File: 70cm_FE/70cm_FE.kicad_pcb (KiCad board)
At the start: 2 copper layers, 50 x 70 mm, 150 parts, among them J2 U.FL, J3 U.FL, J4 U.FL, Q1 2SC3356, Q2 2SC3356, Q3 2SC3356, U1 HT7533-1, U2 74HC14, U3 74HC14, U4 LM393, U5 M68710L

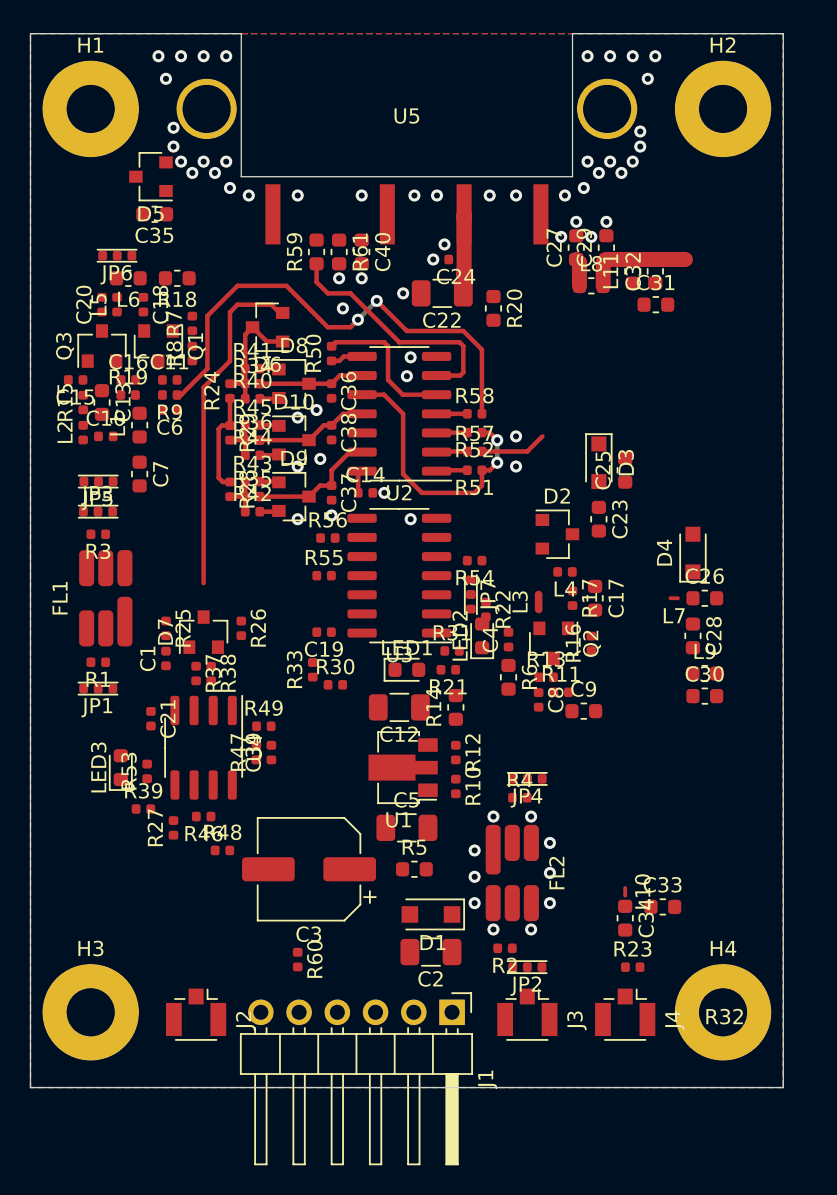
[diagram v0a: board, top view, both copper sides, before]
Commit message: Add RF filtering details and other small additions
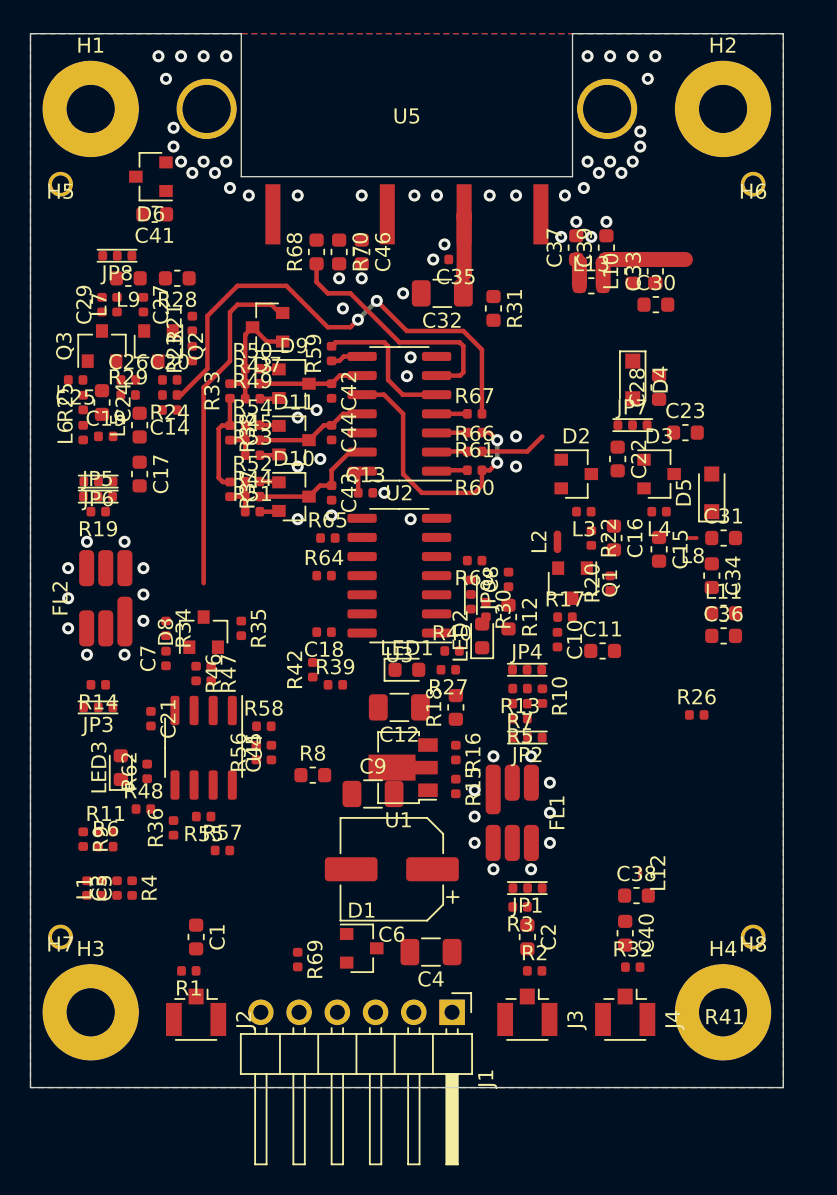
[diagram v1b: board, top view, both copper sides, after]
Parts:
- removed the C4 at (131.8, 90.2)
- added C1: 100p, Capacitor_SMD:C_0603_1608Metric, F.Cu at (111.0, 110.0)
- added C15: 10p, Capacitor_SMD:C_0603_1608Metric, F.Cu at (141.8, 84.2)
- added C2: 100p, Capacitor_SMD:C_0603_1608Metric, F.Cu at (133.0, 110.0)
- added C23: 10p, Capacitor_SMD:C_0603_1608Metric, F.Cu at (143.5, 76.5)
- added C3: 4p7, Capacitor_SMD:C_0402_1005Metric, F.Cu at (105.8, 106.8)
- added C5: DNP, Capacitor_SMD:C_0402_1005Metric, F.Cu at (103.8, 106.8)
- added C8: 1n, Capacitor_SMD:C_0402_1005Metric, F.Cu at (131.8, 86.2)
- added D3: BAV99, Package_TO_SOT_SMD:SOT-23, F.Cu at (141.8, 79.2)
- added H5: Tooling hole, 70cm_FE:JLCPCB_ToolingHole, F.Cu at (102.0, 60.0)
- added H6: Tooling hole, 70cm_FE:JLCPCB_ToolingHole, F.Cu at (148.0, 60.0)
- added H7: Tooling hole, 70cm_FE:JLCPCB_ToolingHole, F.Cu at (102.0, 110.0)
- added H8: Tooling hole, 70cm_FE:JLCPCB_ToolingHole, F.Cu at (148.0, 110.0)
- added JP4: ~, 70cm_FE:Jumper-3_0402, F.Cu at (132.5, 92.2)
- added JP7: ~, 70cm_FE:Jumper-3_0402, F.Cu at (139.5, 76.0)
- added L1: 15n, Inductor_SMD:L_0402_1005Metric, F.Cu at (104.8, 106.8)
- added L4: 15n, Inductor_SMD:L_0402_1005Metric, F.Cu at (141.8, 81.8)
- added R1: 100k, Resistor_SMD:R_0402_1005Metric, F.Cu at (110.5, 112.2)
- added R11: DNP, Resistor_SMD:R_0402_1005Metric, F.Cu at (105.0, 103.0)
- added R13: DNP, Resistor_SMD:R_0402_1005Metric, F.Cu at (132.5, 93.5)
- added R2: 100k, Resistor_SMD:R_0402_1005Metric, F.Cu at (133.5, 112.2)
- added R26: 100k, Resistor_SMD:R_0402_1005Metric, F.Cu at (144.2, 95.2)
- added R4: 47, Resistor_SMD:R_0402_1005Metric, F.Cu at (106.8, 106.8)
- added R6: DNP, Resistor_SMD:R_0402_1005Metric, F.Cu at (105.0, 104.0)
- added R7: DNP, Resistor_SMD:R_0402_1005Metric, F.Cu at (132.5, 94.5)
- added R9: 0, Resistor_SMD:R_0402_1005Metric, F.Cu at (103.5, 103.5)
- C7: renamed from C1; value 1p -> 4p7
- D1: value SM4007PL -> BAV99; footprint Diode_SMD:D_SOD-123F -> Package_TO_SOT_SMD:SOT-23
- D8: renamed from D7; value BAT54C -> BAS70-05
- L12: renamed from L10; value 23 mm -> 22 mm
- L8: renamed from L7; value 24 mm -> 26 mm
- moved R8 9.20 mm to (118.8, 99.2)
- moved C28 5.94 mm to (141.8, 73.5)
- moved D4 5.94 mm to (140.0, 73.0)
- moved C6 5.50 mm to (124.0, 105.5)
- moved JP1 5.25 mm to (133.5, 106.8)
- moved R5 5.25 mm to (132.5, 95.5), turned to 180 degrees
- moved D1 5.12 mm to (122.0, 110.8), turned to 0 degrees
- moved C10 4.19 mm to (135.0, 90.2)
- moved C11 4.19 mm to (138.0, 91.0)
- moved C16 4.19 mm to (138.8, 83.5)
- moved C22 4.19 mm to (139.0, 78.2)
- moved C31 4.19 mm to (146.0, 83.5)
- moved C34 4.19 mm to (145.2, 86.0)
- moved C36 4.19 mm to (146.0, 90.0)
- moved D2 4.19 mm to (136.2, 79.2)
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- renumbered C8 to C10, C9 to C11, C14 to C13, C6 to C14, C17 to C16, C7 to C17, C19 to C18, C10 to C19, C11 to C20, C23 to C22, C13 to C24, C15 to C25, C16 to C26, C18 to C27, C25 to C28, C20 to C29, C31 to C30, C26 to C31, C22 to C32, C32 to C33, C28 to C34, C24 to C35, C30 to C36, C27 to C37, C33 to C38, C29 to C39, C2 to C4, C34 to C40, C35 to C41, C36 to C42, C37 to C43, C38 to C44, C39 to C45, C40 to C46, C3 to C6, C5 to C9, D9 to D10, D10 to D11, D3 to D4, D4 to D5, D5 to D6, D6 to D7, D8 to D9, FL2 to FL1, FL1 to FL2, JP2 to JP1, JP4 to JP2, JP1 to JP3, JP3 to JP5, JP5 to JP6, JP6 to JP8, JP7 to JP9, L11 to L10, L9 to L11, L8 to L13, L3 to L2, L4 to L3, L1 to L5, L2 to L6, L5 to L7, L6 to L9, Q2 to Q1, Q1 to Q2, R11 to R10, R6 to R12, R1 to R14, R10 to R15, R12 to R16, R13 to R17, R14 to R18, R3 to R19, R16 to R20, R7 to R21, R17 to R22, R8 to R23, R9 to R24, R15 to R25, R21 to R27, R18 to R28, R19 to R29, R2 to R3, R22 to R30, R20 to R31, R23 to R32, R24 to R33, R25 to R34, R26 to R35, R27 to R36, R28 to R37, R29 to R38, R30 to R39, R31 to R40, R32 to R41, R33 to R42, R34 to R43, R35 to R44, R36 to R45, R37 to R46, R38 to R47, R39 to R48, R40 to R49, R4 to R5, R41 to R50, R42 to R51, R43 to R52, R44 to R53, R45 to R54, R46 to R55, R47 to R56, R48 to R57, R49 to R58, R50 to R59, R51 to R60, R52 to R61, R53 to R62, R54 to R63, R55 to R64, R56 to R65, R57 to R66, R58 to R67, R59 to R68, R60 to R69, R61 to R70, R5 to R8
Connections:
- C11 pad 1: Net-(C9-Pad1) (its old number) -> /LNA_C
- C22 pad 1: /PIN_RXRF -> /LNA_IN
- C7 pad 1: /TX -> Net-(C5-Pad1)
- D1 pad 1: /V_in -> GND
- D1 pad 2: GND -> /V_in
- JP1 pad 2: /RX -> Net-(C2-Pad1)
- JP2 pad 2: /LNA_OUT -> Net-(JP2-Pad2)
- JP3 pad 1: /TXSAW_in -> /TXSAW_bypass
- JP3 pad 2: /TX -> Net-(JP3-Pad2)
- JP3 pad 3: /TXSAW_bypass -> /TXSAW_in
- JP5 pad 2: Net-(JP3-Pad2) -> /TX_filtered
- JP6 pad 2: Net-(JP3-Pad2) -> /TX_filtered
- R10 pad 1: /LNA_C -> Net-(JP4-Pad2)
- R10 pad 2: Net-(C9-Pad1) (its old number) -> Net-(JP2-Pad2)
- R14 pad 1: /TXSAW_in -> Net-(JP3-Pad2)
- R19 pad 1: /TXSAW_out -> /TX_filtered
- R3 pad 1: /RXSAW_OUT -> Net-(C2-Pad1)
- R5 pad 1: /RXSAW_IN -> Net-(JP2-Pad2)
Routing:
- net GND: vias 66 -> 76

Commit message: Do some layout for 70 cm frontend
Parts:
- moved R41 40.2 mm to (114.0, 92.2), turned to 90 degrees
- moved D8 15.6 mm to (110.2, 105.2), turned to 270 degrees
- moved R40 15.1 mm to (113.0, 92.2), turned to 270 degrees
- moved R35 13.2 mm to (111.8, 102.5)
- moved R34 13.0 mm to (108.8, 102.5)
- moved R57 12.0 mm to (112.0, 92.2), turned to 270 degrees
- moved C7 11.6 mm to (107.2, 103.0), turned to 0 degrees
- moved C45 11.1 mm to (117.2, 86.8)
- moved R56 11.1 mm to (116.2, 86.8)
- moved R36 11.0 mm to (110.5, 91.8), turned to 180 degrees
- moved R46 10.1 mm to (109.8, 102.5), turned to 90 degrees
- moved R47 10.1 mm to (110.8, 102.5), turned to 90 degrees
- moved R48 9.37 mm to (109.0, 92.2), turned to 270 degrees
- moved R55 9.30 mm to (110.5, 92.8)
- moved C21 8.75 mm to (113.2, 102.5)
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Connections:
- D8 pad 1: /DET_RF -> /DET_REF
- D8 pad 2: /DET_REF -> /DET_RF
- U4 pad 1: /DET_COMPout -> /~OverTemp~
- U4 pad 2: /DET_COMP- -> /TempLimit
- U4 pad 3: /DET_COMP+ -> /TempHysteresis
- U4 pad 5: /TempHysteresis -> /DET_COMP+
- U4 pad 6: /TempLimit -> /DET_COMP-
- U4 pad 7: /~OverTemp~ -> /DET_COMPout
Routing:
- net /~OverTemp~: track 22.7 -> 30.4 mm
- net /VDD: track 1.55 -> 7.24 mm
- net /PA_VDD: track 4.32 -> 0.37 mm
- net /TempHysteresis: track 0.00 -> 3.58 mm
- net /TempLimit: track 0.00 -> 3.58 mm
- net /DET_RF: track 0.00 -> 3.47 mm
- net /DET_REF: track 0.00 -> 2.45 mm
- net /DET_COMP+: track 0.00 -> 2.17 mm
- net /DET_COMP-: track 0.00 -> 2.16 mm
- net /TempSensor: track 0.00 -> 1.02 mm
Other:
- outline, holes or cut-outs redrawn

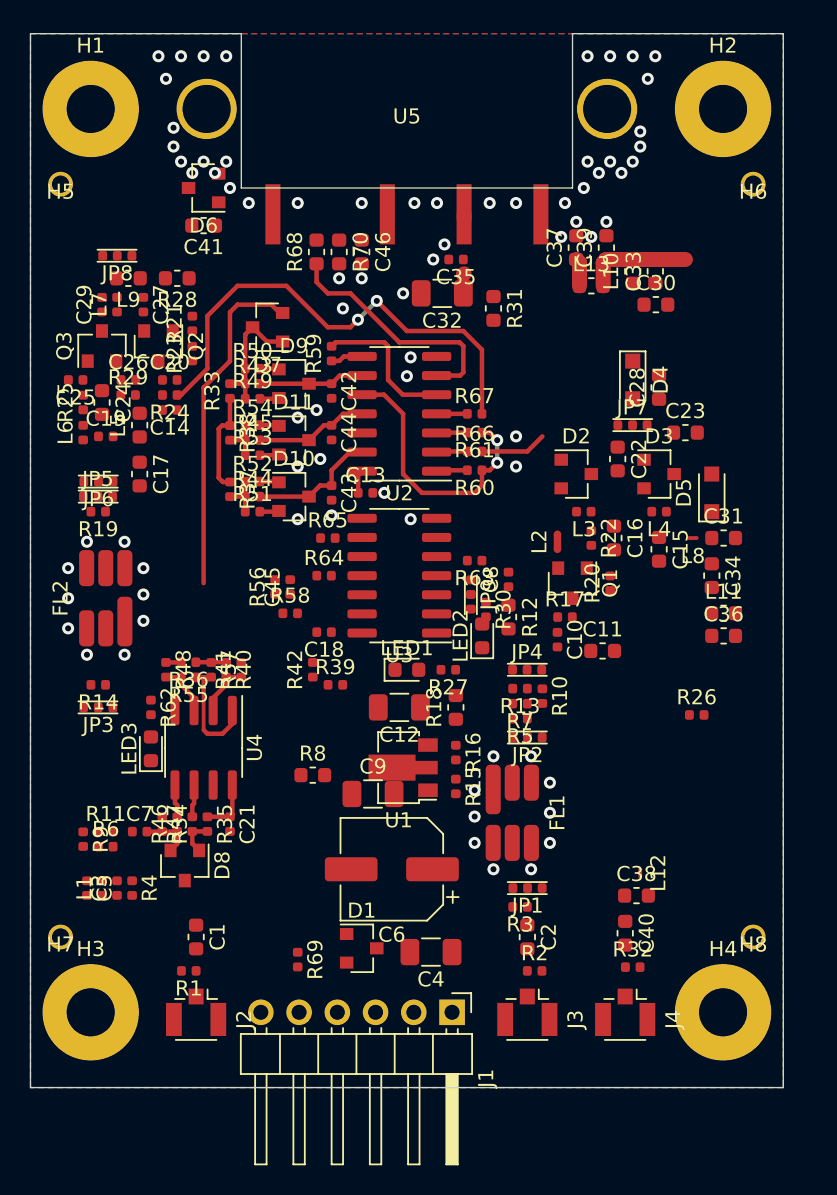
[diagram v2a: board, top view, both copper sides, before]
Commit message: More 70 cm frontend layout
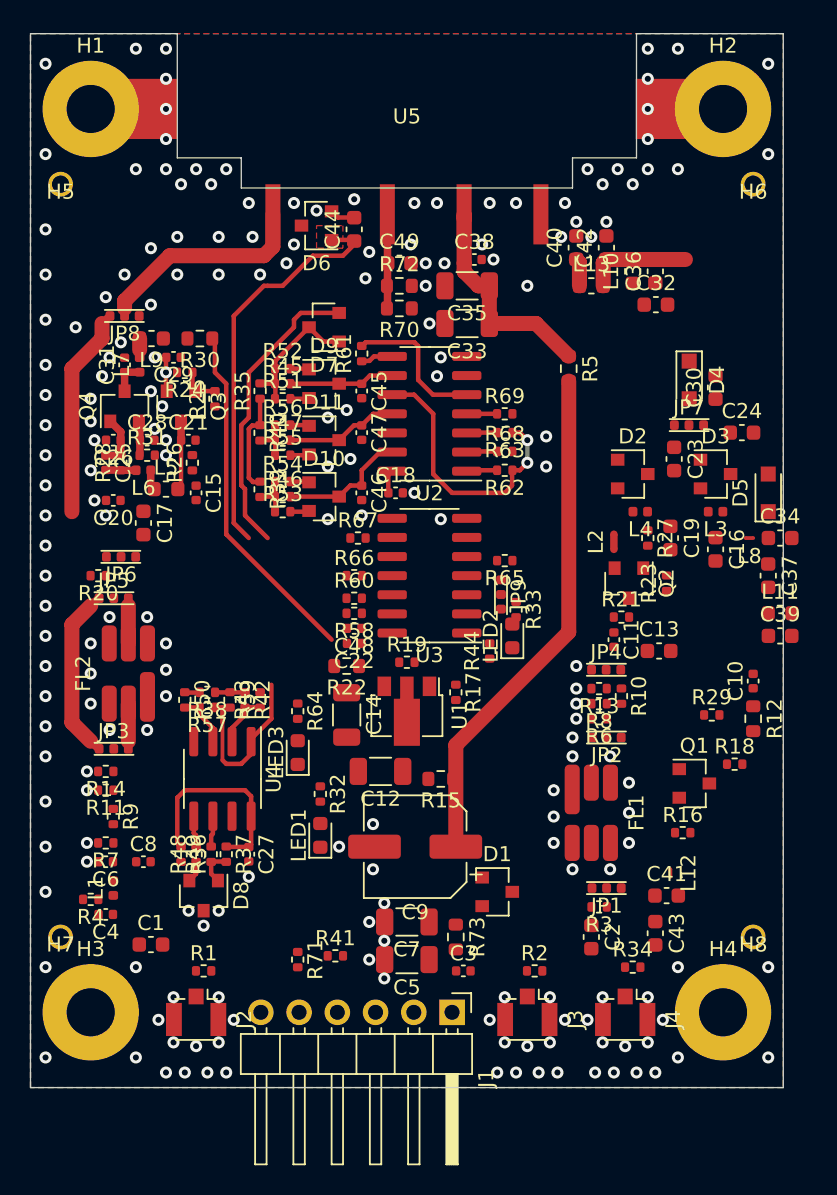
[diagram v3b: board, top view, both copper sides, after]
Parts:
- removed the C14 at (109.2, 75.0)
- removed the C19 at (105.0, 76.8)
- removed the C24 at (104.8, 74.5)
- removed the C8 at (131.8, 86.2)
- removed the Q2 at (108.5, 70.8)
- removed the R19 at (104.5, 81.8)
- removed the R21 at (110.8, 69.2)
- removed the R23 at (110.8, 71.2)
- removed the R29 at (106.5, 74.0)
- removed the R34 at (108.8, 102.5)
- removed the R35 at (111.8, 102.5)
- removed the R40 at (113.0, 92.2)
- removed the R41 at (114.0, 92.2)
- removed the R46 at (109.8, 102.5)
- removed the R47 at (110.8, 102.5)
- removed the R55 at (110.5, 92.8)
- removed the R62 at (108.0, 94.8)
- added C10: 1n, Capacitor_SMD:C_0402_1005Metric, F.Cu at (148.0, 93.0)
- added C15: 1n, Capacitor_SMD:C_0402_1005Metric, F.Cu at (111.0, 80.5)
- added C28: 1n, Capacitor_SMD:C_0402_1005Metric, F.Cu at (107.8, 77.0)
- added C3: 1u, Capacitor_SMD:C_0402_1005Metric, F.Cu at (128.8, 112.2)
- added C31: ?, Capacitor_SMD:C_0402_1005Metric, F.Cu at (106.2, 72.0)
- added C33: 10u, Capacitor_SMD:C_1206_3216Metric, F.Cu at (129.0, 69.2)
- added C5: 10u, Capacitor_SMD:C_1206_3216Metric, F.Cu at (125.0, 111.5)
- added Q1: 2SC3356, Package_TO_SOT_SMD:SOT-23, F.Cu at (144.1, 99.8)
- added Q4: 2SC3356, Package_TO_SOT_SMD:SOT-23, F.Cu at (106.2, 74.8)
- added R16: 47, Resistor_SMD:R_0402_1005Metric, F.Cu at (143.3, 103.1)
- added R18: 100, Resistor_SMD:R_0402_1005Metric, F.Cu at (146.8, 98.5)
- added R20: 100k, Resistor_SMD:R_0402_1005Metric, F.Cu at (104.5, 86.0)
- added R26: 1k, Resistor_SMD:R_0402_1005Metric, F.Cu at (110.8, 78.5)
- added R30: 1, Resistor_SMD:R_0603_1608Metric, F.Cu at (111.2, 70.2)
- added R31: 10, Resistor_SMD:R_0402_1005Metric, F.Cu at (107.8, 78.0)
- added R37: 220k, Resistor_SMD:R_0402_1005Metric, F.Cu at (113.0, 104.5)
- added R38: 100k, Resistor_SMD:R_0402_1005Metric, F.Cu at (111.8, 93.8)
- added R42: 100k, Resistor_SMD:R_0402_1005Metric, F.Cu at (114.2, 94.2)
- added R43: 22k, Resistor_SMD:R_0402_1005Metric, F.Cu at (115.2, 94.2)
- added R49: 1k, Resistor_SMD:R_0402_1005Metric, F.Cu at (112.0, 104.5)
- added R50: 1k, Resistor_SMD:R_0402_1005Metric, F.Cu at (110.2, 94.2)
- added R59: 100k, Resistor_SMD:R_0402_1005Metric, F.Cu at (113.2, 94.2)
- added R64: 10k, Resistor_SMD:R_0402_1005Metric, F.Cu at (117.8, 95.0)
- added R73: 0, Resistor_SMD:R_0603_1608Metric, F.Cu at (128.2, 110.0)
- C20: value 1n -> 10p
- C21: value 100n -> 1n
- C25: value ? -> 10p (?)
- C26: value 1n -> ?
- C27: value 1n -> 100n
- C29: value ? -> 1n
- C38: renamed from C35; value 100n -> 1u
- R21: renamed from R17; value 68 -> 100
- R24: value 1k -> 4k7
- R25: value 100 -> 1k
- R28: value 1 -> 100; footprint Resistor_SMD:R_0603_1608Metric -> Resistor_SMD:R_0402_1005Metric
- R57: value 100k -> 220k
- moved C27 37.2 mm to (114.5, 104.5)
- moved C21 25.6 mm to (110.5, 77.0), turned to 0 degrees
- moved R41 18.0 mm to (120.2, 111.2)
- moved R12 17.6 mm to (148.0, 95.5)
- moved R28 12.8 mm to (106.0, 78.5), turned to 90 degrees
- moved R36 12.8 mm to (110.0, 104.5), turned to 270 degrees
- moved LED1 12.4 mm to (119.2, 103.2), turned to 90 degrees
- moved R48 12.4 mm to (111.0, 104.5), turned to 90 degrees
- moved R32 11.8 mm to (119.2, 100.5), turned to 270 degrees
- moved R44 11.8 mm to (130.5, 91.0)
- moved C44 10.0 mm to (121.5, 63.0), turned to 90 degrees
- moved LED3 9.75 mm to (117.8, 97.8)
- moved D1 9.75 mm to (131.0, 107.0)
- moved C20 8.84 mm to (105.5, 81.0), turned to 180 degrees
- moved R25 8.75 mm to (112.2, 74.2)
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- renumbered C10 to C11, C9 to C12, C11 to C13, C12 to C14, C15 to C16, C13 to C18, C16 to C19, C18 to C22, C22 to C23, C23 to C24, C28 to C30, C30 to C32, C31 to C34, C32 to C35, C33 to C36, C34 to C37, C36 to C39, C3 to C4, C37 to C40, C38 to C41, C39 to C42, C40 to C43, C41 to C44, C42 to C45, C43 to C46, C44 to C47, C45 to C48, C46 to C49, C5 to C6, C4 to C7, C7 to C8, C6 to C9, L4 to L3, L3 to L4, Q1 to Q2, R8 to R15, R15 to R17, R16 to R19, R18 to R22, R20 to R23, R22 to R27, R26 to R29, R27 to R32, R30 to R33, R32 to R34, R33 to R35, R37 to R39, R38 to R40, R39 to R41, R42 to R44, R43 to R45, R44 to R46, R45 to R47, R31 to R5, R49 to R51, R50 to R52, R51 to R53, R52 to R54, R53 to R55, R54 to R56, R56 to R58, R5 to R6, R58 to R60, R59 to R61, R60 to R62, R61 to R63, R63 to R65, R64 to R66, R65 to R67, R66 to R68, R67 to R69, R6 to R7, R68 to R70, R69 to R71, R70 to R72, R7 to R8
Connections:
- net Net-(C9-Pad1) renamed /REG_in
- net Net-(R15-Pad1) renamed /REG_GND
- C13 pad 1: /LNA_C -> Net-(C13-Pad1)
- C20 pad 1: /DRV_bias -> Net-(C17-Pad1)
- C21 pad 1: /VDD -> /DRV_bias
- C25 pad 2: GND -> Net-(C25-Pad2)
- C26 pad 1: /DRV_E -> /DRV_B
- C27 pad 1: Net-(C27-Pad1) -> /VDD
- C29 pad 1: /DRV_C -> Net-(C29-Pad1)
- J1 pad 1: /V_in -> /V_in1
- L6 pad 2: Net-(C24-Pad2) -> Net-(C25-Pad2)
- L9 pad 1: Net-(C27-Pad1) -> Net-(C29-Pad1)
- Q3 pad 1: /DRV_B -> Net-(Q3-Pad1)
- Q3 pad 2: /DRV_E -> GND
- Q3 pad 3: /DRV_C -> /DRV_bias
- R24 pad 1: /DRV_EN -> Net-(Q3-Pad1)
- R24 pad 2: /DRV_bias -> GND
- R25 pad 1: Net-(C24-Pad2) -> /DRV_bias
- R25 pad 2: /DRV_B -> Net-(Q3-Pad1)
- R28 pad 1: /VDD -> Net-(C25-Pad2)
- R28 pad 2: Net-(C27-Pad1) -> /DRV_B
- R36 pad 2: /TempSensor -> /DET_RF
- R48 pad 1: /TempSensor -> /DET_RF
- R48 pad 2: /TempHysteresis -> /DET_COMP+
- R57 pad 1: /VDD -> /~OverTemp~
- R57 pad 2: /~OverTemp~ -> /TempHysteresis
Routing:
- net /V_in: track 0.00 -> 34.0 mm
- net /VDD: track 7.24 -> 40.5 mm
- net /DRV_EN: track 32.8 -> 0.00 mm, vias 2 -> 0
- net /TempSensor: track 1.02 -> 27.7 mm
- net /PA_EN: track 16.3 -> 0.00 mm
- net /PA_in: track 0.00 -> 14.5 mm
- net /PA_VDD: track 0.37 -> 14.8 mm
- net /DRV_bypass: track 0.00 -> 14.1 mm
- net /TXSAW_bypass: track 0.00 -> 11.6 mm
- net /PA_VGG: track 0.00 -> 6.26 mm
- net /DRV_bias: track 0.00 -> 4.59 mm
- net /PIN_bias: track 4.43 -> 0.00 mm
- net GND: track 0.00 -> 3.95 mm, vias 76 -> 192
- net /DRV_B: track 0.00 -> 3.56 mm
- net Net-(Q3-Pad1): track 0.00 -> 2.63 mm
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- added copper zone on F.Cu, net /TempSensor
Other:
- outline, holes or cut-outs redrawn
